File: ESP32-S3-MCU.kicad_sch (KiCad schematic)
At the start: 34 parts, among them SW1 RESET, SW2 BOOT, U1 ESP32-S3FH4R2, Y1 Crystal_GND24_Small

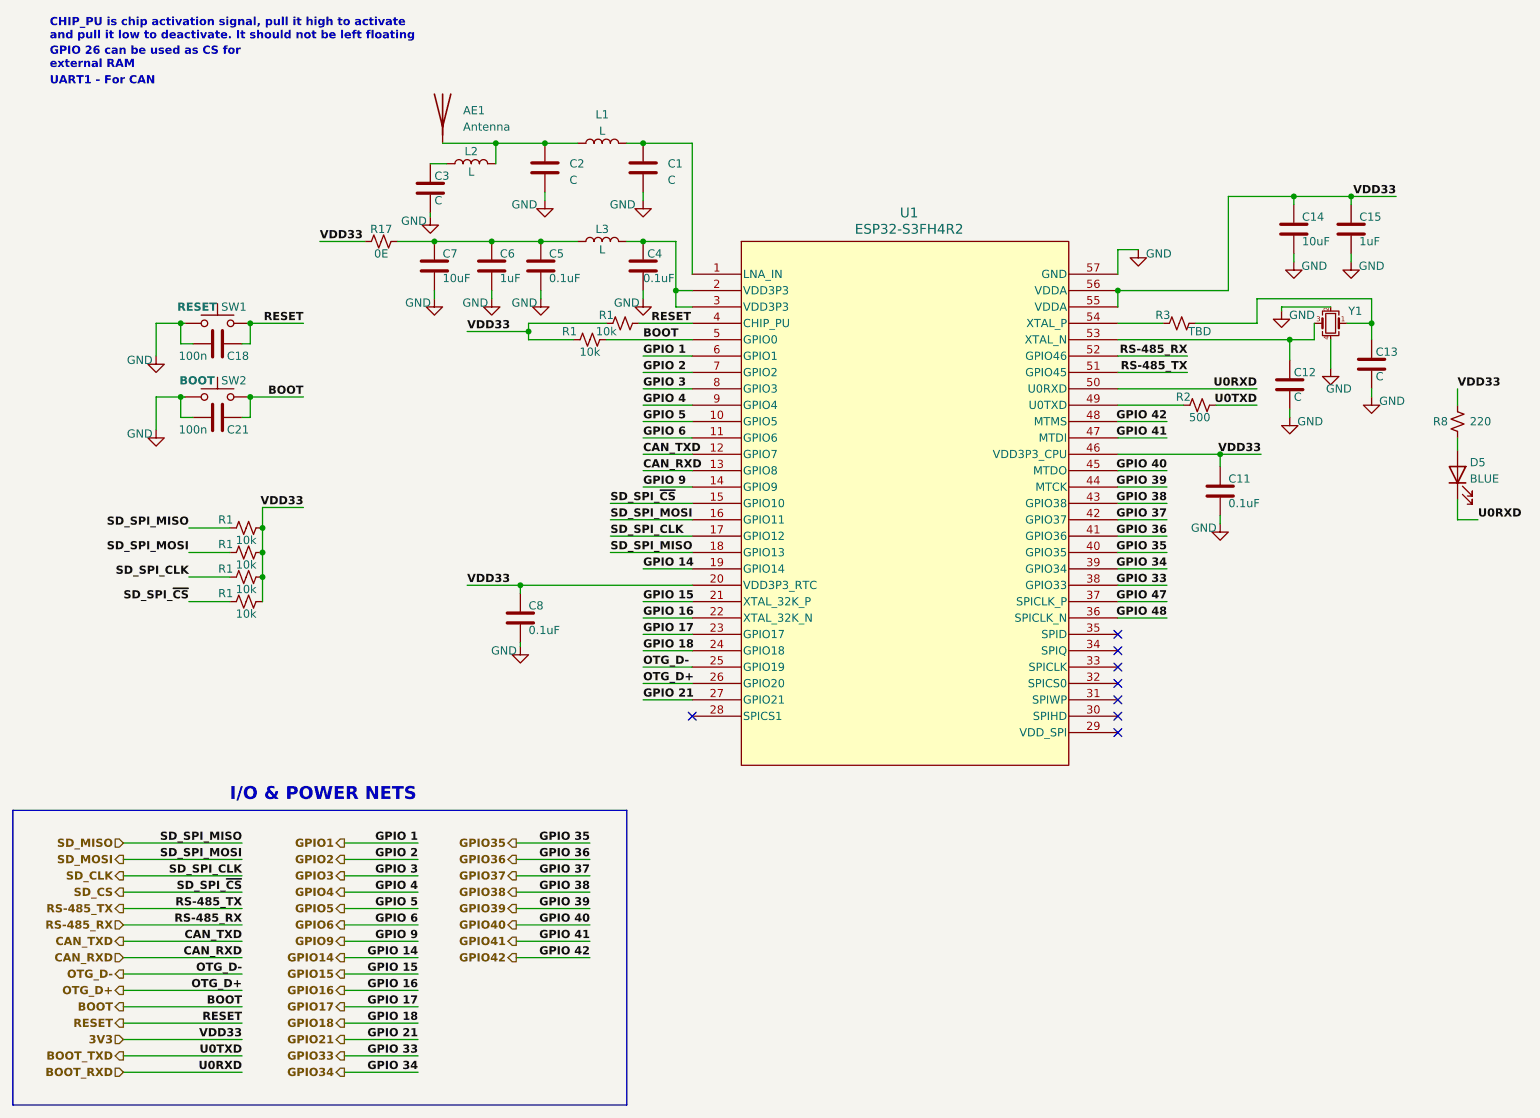
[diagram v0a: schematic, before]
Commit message: Completed header connections
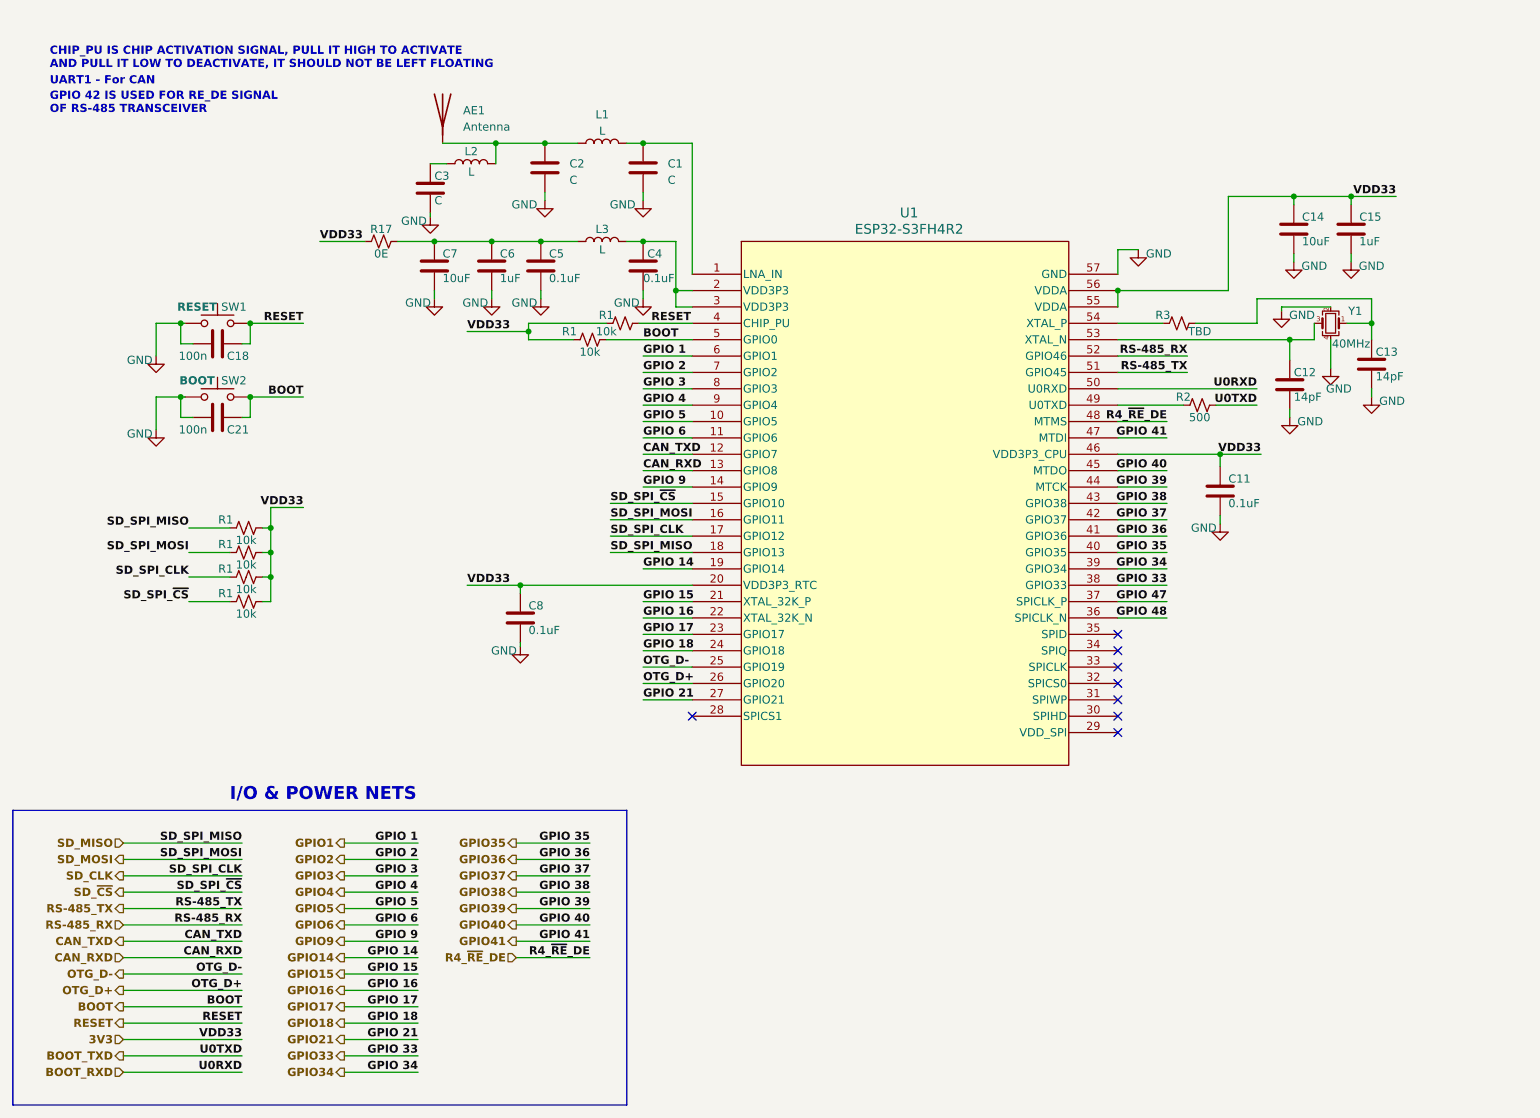
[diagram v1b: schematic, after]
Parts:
- removed D5: BLUE, symbol ESP32-S3_DB:LED
- removed R8: 220, symbol ESP32-S3_DB:R_Small_US
- C12, C13: value C -> 14pF
- Y1: value Crystal_GND24_Small -> 40MHz; PN (none) -> SX3B40.000F1210F30
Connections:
- net GPIO42 renamed R4_~{RE}_DE
- net SD_CS renamed SD_~{CS}
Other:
- note added: "CHIP_PU IS CHIP ACTIVATION SIGNAL, PULL IT HIGH TO ACTIVATE AND PULL IT LOW TO DEACTIVATE, IT SHOULD NOT BE LEFT FLOATING"
- note added: "GPIO 42 IS USED FOR RE_DE SIGNAL OF RS-485 TRANSCEIVER"
- note removed: "CHIP_PU is chip activation signal, pull it high to activate and pull it low to deactivate. It should not be left floating"
- note removed: "GPIO 26 can be used as CS for external RAM"

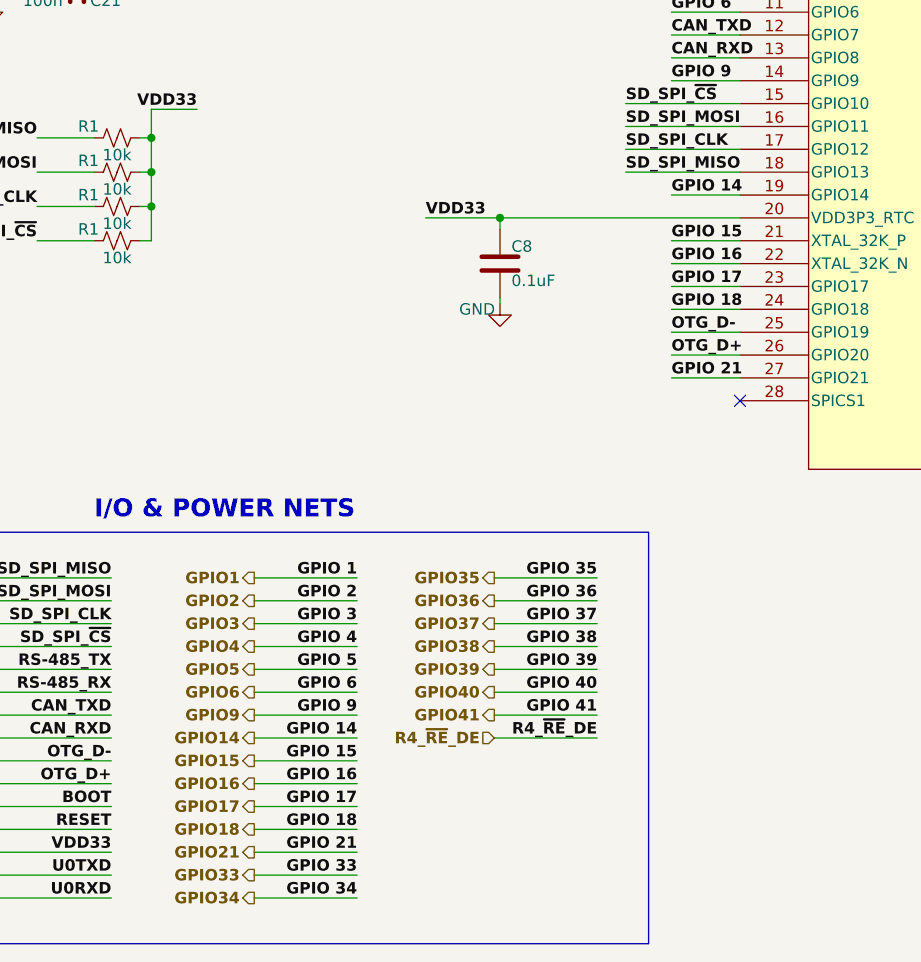
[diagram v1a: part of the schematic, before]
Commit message: Added 32.768KHz crystal for lower power usage
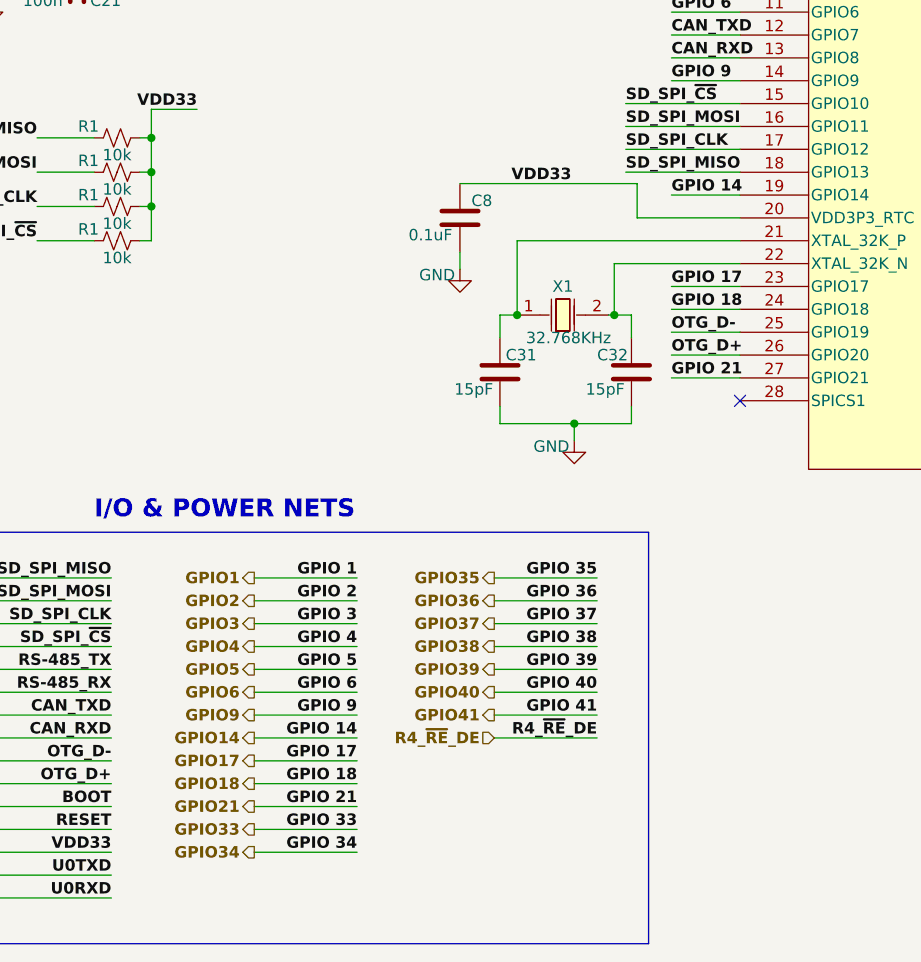
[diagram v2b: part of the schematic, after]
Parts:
- added C31, C32: 15pF, symbol ESP32-S3_DB:C
- added X1: 32.768KHz, easyeda2kicad:CRYSTAL-SMD_L3.2-W1.5, symbol ESP32-S3_DB:AH03200003
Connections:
- net GND: now also C31.2, C32.2
- net GPIO15: no longer names the net of U1.21 (XTAL_32K_P)
- net GPIO15: now also C31.1, X1.1
- net GPIO16: no longer names the net of U1.22 (XTAL_32K_N)
- net GPIO16: now also C32.1, X1.2
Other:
- moved on the sheet: C8

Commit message: Assigned PN and Footprint for C
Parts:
- added C6, C8: 1uF, ESP32-S3_DB:C_0603_1608Metric, symbol ESP32-S3_DB:C
- added C7: 10uF, ESP32-S3_DB:C_0805_2012Metric, symbol ESP32-S3_DB:C
- C11, C4, C5, C8: value 0.1uF -> 100nF; footprint (none) -> ESP32-S3_DB:C_0402_1005Metric; PN (none) -> EMK107B7104KAHT
- C14, C7: footprint (none) -> ESP32-S3_DB:C_0805_2012Metric; PN (none) -> CL21A106KAYNNNE
- C15, C6: footprint (none) -> ESP32-S3_DB:C_0603_1608Metric; PN (none) -> CC0603KRX5R8BB105
- C18, C21: value 100n -> 100nF; footprint (none) -> ESP32-S3_DB:C_0402_1005Metric; PN (none) -> EMK107B7104KAHT
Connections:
- net 3V3: now also C6.1, C7.1, C8.1
- net GND: now also C6.2, C7.2, C8.2

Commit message: Assigned footprints
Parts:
- C11, C18, C21, C4, C5, C8: footprint ESP32-S3_DB:C_0402_1005Metric -> ESP32-S3_Dev_Board:C_0402_1005Metric
- C14, C7: footprint ESP32-S3_DB:C_0805_2012Metric -> ESP32-S3_Dev_Board:C_0805_2012Metric
- C15, C6, C8: footprint ESP32-S3_DB:C_0603_1608Metric -> ESP32-S3_Dev_Board:C_0603_1608Metric
- R1: footprint (none) -> ESP32-S3_Dev_Board:R_0402_1005Metric; PN (none) -> RC0402FR-0710KL
- R17: footprint (none) -> ESP32-S3_Dev_Board:R_0603_1608Metric; PN (none) -> RC0603JR-070RL
- R2: footprint (none) -> ESP32-S3_Dev_Board:R_0402_1005Metric; PN (none) -> RC0402FR-07499RL
- SW1, SW2: footprint (none) -> ESP32-S3_Dev_Board:KEY-SMD_4P-L5.2-W5.2-P3.70-LS6.4; PN (none) -> K2-1187SQ-A4SW-06
- U1: footprint QFN56_7X7_EXP -> ESP32-S3_Dev_Board:QFN-56_L7.0-W7.0-P0.40-TL-EP4.0
- X1: footprint easyeda2kicad:CRYSTAL-SMD_L3.2-W1.5 -> ESP32-S3_Dev_Board:CRYSTAL-SMD_L3.2-W1.5
- Y1: footprint (none) -> ESP32-S3_Dev_Board:CRYSTAL-SMD_4P-L3.2-W2.5-BL
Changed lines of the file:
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@@
       (effects (font (size 1.27 1.27)))
     )
-    (property "Footprint" "" (at 73.025 57.15 0)
+    (property "Footprint" "ESP32-S3_Dev_Board:R_0603_1608Metric" (at 73.025 57.15 0)
       (effects (font (size 1.27 1.27)) hide)
     )
@@
       (effects (font (size 1.27 1.27)) hide)
     )
+    (property "PN" "RC0603JR-070RL" (at 73.025 57.15 0)
+      (effects (font (size 1.27 1.27)) hide)
+    )
     (pin "1")
     (pin "2")
@@
       (effects (font (size 1.27 1.27)))
     )
-    (property "Footprint" "ESP32-S3_DB:C_0402_1005Metric" (at 51.435 72.0598 0)
+    (property "Footprint" "ESP32-S3_Dev_Board:C_0402_1005Metric" (at 51.435 72.0598 0)
       (effects (font (size 1.27 1.27)) hide)
     )
@@
       (effects (font (size 1.27 1.27)))
     )
-    (property "Footprint" "" (at 52.07 105.41 0)
+    (property "Footprint" "ESP32-S3_Dev_Board:R_0402_1005Metric" (at 52.07 105.41 0)
       (effects (font (size 1.27 1.27)) hide)
     )
@@
       (effects (font (size 1.27 1.27)) hide)
     )
+    (property "PN" "RC0402FR-0710KL" (at 52.07 105.41 0)
+      (effects (font (size 1.27 1.27)) hide)
+    )
     (pin "1")
     (pin "2")
@@
       (effects (font (size 1.27 1.27)) (justify left))
     )
-    (property "Footprint" "ESP32-S3_DB:C_0402_1005Metric" (at 98.7552 64.77 0)
+    (property "Footprint" "ESP32-S3_Dev_Board:C_0402_1005Metric" (at 98.7552 64.77 0)
       (effects (font (size 1.27 1.27)) hide)
     )
@@
       (effects (font (size 1.27 1.27)) (justify left))
     )
-    (property "Footprint" "ESP32-S3_DB:C_0603_1608Metric" (at 81.6102 114.3 0)
+    (property "Footprint" "ESP32-S3_Dev_Board:C_0603_1608Metric" (at 81.6102 114.3 0)
       (effects (font (size 1.27 1.27)) hide)
     )
@@
       (effects (font (size 1.27 1.27)))
     )
-    (property "Footprint" "" (at 52.07 113.03 0)
+    (property "Footprint" "ESP32-S3_Dev_Board:R_0402_1005Metric" (at 52.07 113.03 0)
       (effects (font (size 1.27 1.27)) hide)
     )
     (property "Datasheet" "~" (at 52.07 113.03 0)
+      (effects (font (size 1.27 1.27)) hide)
+    )
+    (property "PN" "RC0402FR-0710KL" (at 52.07 113.03 0)
       (effects (font (size 1.27 1.27)) hide)
     )
@@
       (effects (font (size 1.27 1.27)))
     )
-    (property "Footprint" "ESP32-S3_DB:C_0402_1005Metric" (at 51.435 83.4898 0)
+    (property "Footprint" "ESP32-S3_Dev_Board:C_0402_1005Metric" (at 51.435 83.4898 0)
       (effects (font (size 1.27 1.27)) hide)
     )
@@
       (effects (font (size 1.27 1.27)))
     )
-    (property "Footprint" "" (at 220.345 69.85 0)
+    (property "Footprint" "ESP32-S3_Dev_Board:CRYSTAL-SMD_4P-L3.2-W2.5-BL" (at 220.345 69.85 0)
       (effects (font (size 1.27 1.27)) hide)
     )
@@
       (effects (font (size 1.27 1.27)) (justify left))
     )
-    (property "Footprint" "ESP32-S3_DB:C_0402_1005Metric" (at 204.1652 99.695 0)
+    (property "Footprint" "ESP32-S3_Dev_Board:C_0402_1005Metric" (at 204.1652 99.695 0)
       (effects (font (size 1.27 1.27)) hide)
     )
@@
       (effects (font (size 1.27 1.27)))
     )
-    (property "Footprint" "" (at 52.07 109.22 0)
+    (property "Footprint" "ESP32-S3_Dev_Board:R_0402_1005Metric" (at 52.07 109.22 0)
       (effects (font (size 1.27 1.27)) hide)
     )
@@
       (effects (font (size 1.27 1.27)) hide)
     )
+    (property "PN" "RC0402FR-0710KL" (at 52.07 109.22 0)
+      (effects (font (size 1.27 1.27)) hide)
+    )
     (pin "1")
     (pin "2")
@@
       (effects (font (size 1.27 1.27)) (justify left))
     )
-    (property "Footprint" "ESP32-S3_DB:C_0603_1608Metric" (at 91.1352 64.77 0)
+    (property "Footprint" "ESP32-S3_Dev_Board:C_0603_1608Metric" (at 91.1352 64.77 0)
       (effects (font (size 1.27 1.27)) hide)
     )
@@
       (effects (font (size 1.27 1.27)))
     )
-    (property "Footprint" "" (at 200.025 82.55 0)
+    (property "Footprint" "ESP32-S3_Dev_Board:R_0402_1005Metric" (at 200.025 82.55 0)
       (effects (font (size 1.27 1.27)) hide)
     )
@@
       (effects (font (size 1.27 1.27)) hide)
     )
+    (property "PN" "RC0402FR-07499RL" (at 200.025 82.55 0)
+      (effects (font (size 1.27 1.27)) hide)
+    )
     (pin "1")
     (pin "2")
@@
       (effects (font (size 1.27 1.27)) (justify left))
     )
-    (property "Footprint" "ESP32-S3_DB:C_0805_2012Metric" (at 82.2452 64.77 0)
+    (property "Footprint" "ESP32-S3_Dev_Board:C_0805_2012Metric" (at 82.2452 64.77 0)
       (effects (font (size 1.27 1.27)) hide)
     )
@@
       (effects (font (size 1.27 1.27)) (justify left))
     )
-    (property "Footprint" "ESP32-S3_DB:C_0603_1608Metric" (at 224.4852 59.055 0)
+    (property "Footprint" "ESP32-S3_Dev_Board:C_0603_1608Metric" (at 224.4852 59.055 0)
       (effects (font (size 1.27 1.27)) hide)
     )
@@
       (effects (font (size 1.27 1.27)) (justify left))
     )
-    (property "Footprint" "ESP32-S3_DB:C_0805_2012Metric" (at 214.3252 99.695 0)
+    (property "Footprint" "ESP32-S3_Dev_Board:C_0805_2012Metric" (at 214.3252 99.695 0)
       (effects (font (size 1.27 1.27)) hide)
     )
@@
       (effects (font (size 1.27 1.27) bold (color 0 132 0 1)))
     )
-    (property "Footprint" "" (at 47.625 76.2 0)
+    (property "Footprint" "ESP32-S3_Dev_Board:KEY-SMD_4P-L5.2-W5.2-P3.70-LS6.4" (at 47.625 76.2 0)
       (effects (font (size 1.27 1.27)) hide)
     )
@@
       (effects (font (size 1.27 1.27)) hide)
     )
+    (property "PN" "K2-1187SQ-A4SW-06" (at 47.625 81.28 0)
+      (effects (font (size 1.27 1.27)) hide)
+    )
     (pin "1")
     (pin "2")
@@
       (effects (font (size 1.27 1.27)))
     )
-    (property "Footprint" "easyeda2kicad:CRYSTAL-SMD_L3.2-W1.5" (at 101.6 128.905 0)
+    (property "Footprint" "ESP32-S3_Dev_Board:CRYSTAL-SMD_L3.2-W1.5" (at 101.6 128.905 0)
       (effects (font (size 1.27 1.27)) hide)
     )
@@
       (effects (font (size 1.27 1.27)))
     )
-    (property "Footprint" "" (at 52.07 101.6 0)
+    (property "Footprint" "ESP32-S3_Dev_Board:R_0402_1005Metric" (at 52.07 101.6 0)
       (effects (font (size 1.27 1.27)) hide)
     )
@@
       (effects (font (size 1.27 1.27)) hide)
     )
+    (property "PN" "RC0402FR-0710KL" (at 52.07 101.6 0)
+      (effects (font (size 1.27 1.27)) hide)
+    )
     (pin "1")
     (pin "2")
@@
       (effects (font (size 1.27 1.27)) (justify left))
     )
-    (property "Footprint" "ESP32-S3_DB:C_0402_1005Metric" (at 91.1352 114.3 0)
+    (property "Footprint" "ESP32-S3_Dev_Board:C_0402_1005Metric" (at 91.1352 114.3 0)
       (effects (font (size 1.27 1.27)) hide)
     )
@@
       (effects (font (size 1.27 1.27)))
     )
-    (property "Footprint" "" (at 110.49 69.85 0)
+    (property "Footprint" "ESP32-S3_Dev_Board:R_0402_1005Metric" (at 110.49 69.85 0)
       (effects (font (size 1.27 1.27)) hide)
     )
     (property "Datasheet" "~" (at 110.49 69.85 0)
+      (effects (font (size 1.27 1.27)) hide)
+    )
+    (property "PN" "RC0402FR-0710KL" (at 110.49 69.85 0)
       (effects (font (size 1.27 1.27)) hide)
     )
@@
       (effects (font (size 1.524 1.524)))
     )
-    (property "Footprint" "QFN56_7X7_EXP" (at 154.94 85.09 0) (do_not_autoplace)
+    (property "Footprint" "ESP32-S3_Dev_Board:QFN-56_L7.0-W7.0-P0.40-TL-EP4.0" (at 154.94 85.09 0) (do_not_autoplace)
       (effects (font (size 1.27 1.27) italic) hide)
     )
@@
       (effects (font (size 1.27 1.27) bold (color 0 132 0 1)))
     )
-    (property "Footprint" "" (at 47.625 64.77 0)
+    (property "Footprint" "ESP32-S3_Dev_Board:KEY-SMD_4P-L5.2-W5.2-P3.70-LS6.4" (at 47.625 64.77 0)
       (effects (font (size 1.27 1.27)) hide)
     )
@@
       (effects (font (size 1.27 1.27)) hide)
     )
+    (property "PN" "K2-1187SQ-A4SW-06" (at 47.625 69.85 0)
+      (effects (font (size 1.27 1.27)) hide)
+    )
     (pin "1")
     (pin "2")
@@
       (effects (font (size 1.27 1.27)) (justify left))
     )
-    (property "Footprint" "ESP32-S3_DB:C_0402_1005Metric" (at 114.6302 64.77 0)
+    (property "Footprint" "ESP32-S3_Dev_Board:C_0402_1005Metric" (at 114.6302 64.77 0)
       (effects (font (size 1.27 1.27)) hide)
     )
@@
       (effects (font (size 1.27 1.27)))
     )
-    (property "Footprint" "" (at 105.41 72.39 0)
+    (property "Footprint" "ESP32-S3_Dev_Board:R_0402_1005Metric" (at 105.41 72.39 0)
       (effects (font (size 1.27 1.27)) hide)
     )
@@
       (effects (font (size 1.27 1.27)) hide)
     )
+    (property "PN" "RC0402FR-0710KL" (at 105.41 72.39 0)
+      (effects (font (size 1.27 1.27)) hide)
+    )
     (pin "1")
     (pin "2")
@@
       (effects (font (size 1.27 1.27)) (justify left))
     )
-    (property "Footprint" "ESP32-S3_DB:C_0603_1608Metric" (at 223.2152 99.695 0)
+    (property "Footprint" "ESP32-S3_Dev_Board:C_0603_1608Metric" (at 223.2152 99.695 0)
       (effects (font (size 1.27 1.27)) hide)
     )
@@
       (effects (font (size 1.27 1.27)) (justify left))
     )
-    (property "Footprint" "ESP32-S3_DB:C_0805_2012Metric" (at 215.5952 59.055 0)
-      (effects (font (size 1.27 1.27)) hide)
-    )
+    (property "Footprint" "ESP32-S3_Dev_Board:C_0805_2012Metric" (at 215.5952 59.055 0)
+      (effects (font (size 1.27 1.27)) hide)
+    )

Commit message: Screw Terminal FPs
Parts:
- U1: PN (none) -> ESP32-S3FH4R2
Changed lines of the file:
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@@
       (effects (font (size 1.27 1.27) italic) hide)
+    )
+    (property "PN" "ESP32-S3FH4R2" (at 121.285 62.23 0)
+      (effects (font (size 1.27 1.27)) hide)
     )
     (pin "1")
